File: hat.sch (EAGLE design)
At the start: 43 parts, among them U1 ADS1115IDGST, U2 ADXL345, U3 MCP2515-I/SO, U4 MCP2551, X1 16Mhz

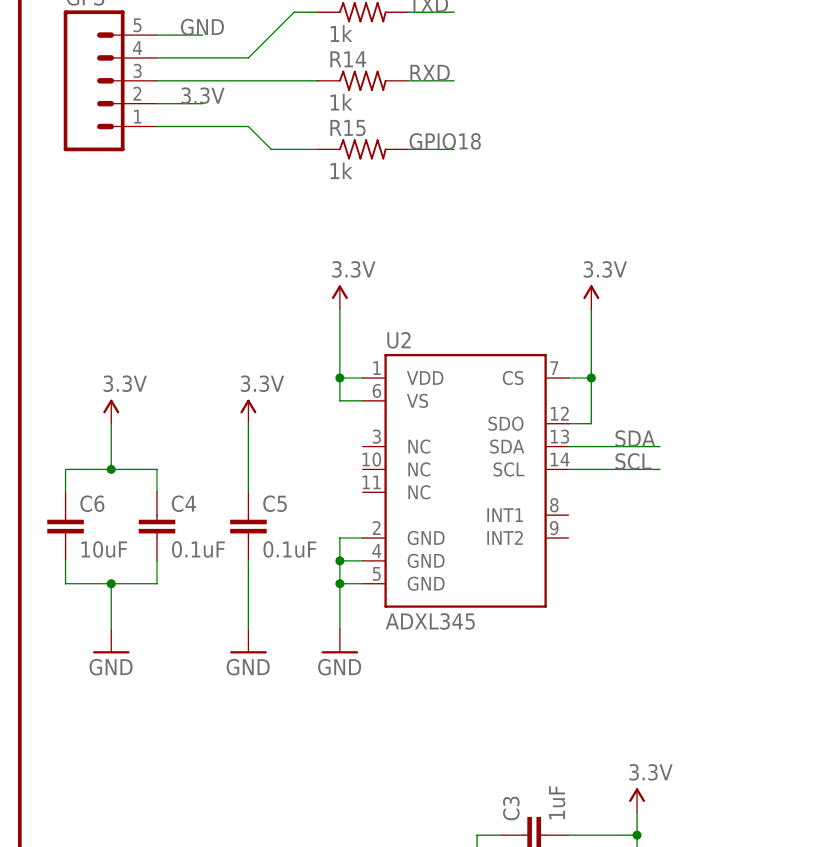
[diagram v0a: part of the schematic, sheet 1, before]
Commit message: Replaced accelerometer with i2c header
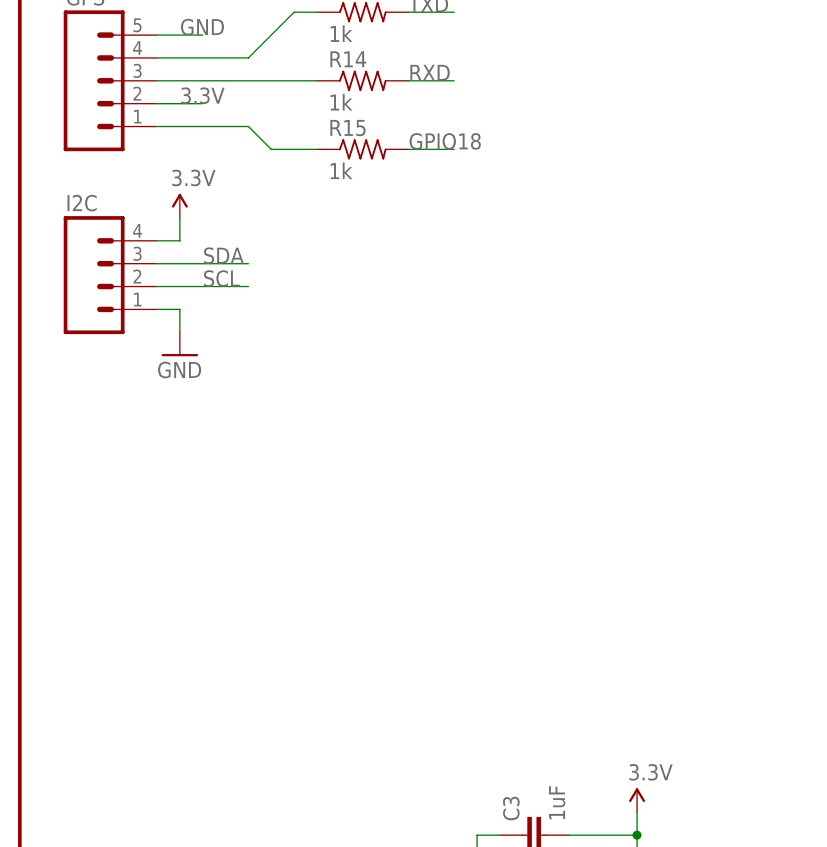
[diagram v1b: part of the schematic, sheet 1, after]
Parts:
- removed C10: 0.1uF, aceat64-passives:CAPACITOR_C0805
- removed C11, C12: 22pF, aceat64-passives:CAPACITOR_C0805
- removed U4: MCP2551, SparkFun-DigitalIC:MCP2551
- added I2C: (no value), SparkFun-Connectors:M04PTH
- C4, C5: value 0.1uF -> 560pF
- C6: value 10uF -> 0.1uF
- C7: value 560pF -> 0.1uF
- C8: value 560pF -> 22pF
- C9: value 0.1uF -> 22pF
- U2: value ADXL345 -> MCP2515-I/SO; device SparkFun-Sensors:ADXL345 -> mcp2515:MCP2515-I/SO
- U3: value MCP2515-I/SO -> MCP2551; device mcp2515:MCP2515-I/SO -> SparkFun-DigitalIC:MCP2551
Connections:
- net 3.3V: now also C7.1, I2C.4; no longer C10.1, C4.1, C5.1, C6.1, U2.CS, U2.SDO, U2.VS, U3.VDD
- net 5V: now also C6.1, U3.VSS; no longer C9.1, U4.VSS
- net CANH: now also U3.CANH; no longer U4.CANH
- net CANL: now also U3.CANL; no longer U4.CANL
- net GND: now also I2C.1, U2.VSS, U3.VDD; no longer C10.2, C11.2, C12.2, U2.GND@2, U2.GND@4, U2.GND@5, U3.VSS, U4.VDD
- net GPIO25: now also U2.INT; no longer U3.INT
- net N$14: now also C9.1, U2.OSC1; no longer C12.1, U3.OSC1
- net N$15: now also C8.1, U2.OSC2; no longer C11.1, U3.OSC2
- net N$4: now also U2.RXCAN; no longer U3.RXCAN
- net N$6: now also C4.1; no longer C7.1
- net N$8: now also C5.1; no longer C8.1
- net RS: now also U3.RS; no longer U4.RS
- net RXCAN: now also U3.RXD; no longer U4.RXD
- net SCL: now also I2C.2; no longer U2.SCL
- net SDA: now also I2C.3; no longer U2.SDA
- net SPI_CE0: now also U2.CS; no longer U3.CS
- net SPI_MISO: now also U2.SO; no longer U3.SO
- net SPI_MOSI: now also U2.SI; no longer U3.SI
- net SPI_SCLK: now also U2.SCK; no longer U3.SCK
- net TXCAN: now also U2.TXCAN, U3.TXD; no longer U3.TXCAN, U4.TXD
- net U5_RST: now also U2.RESET; no longer U3.RESET
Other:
- moved on the sheet: C7, C8, C9

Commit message: Rename U5_RST to U2_RST
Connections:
- net U5_RST renamed U2_RST
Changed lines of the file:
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@@
 <grid distance="0.1" unitdist="inch" unit="inch" style="lines" multiple="1" display="no" altdistance="0.01" altunitdist="inch" altunit="inch"/>
 <layers>
-<layer number="1" name="Top" color="4" fill="1" visible="yes" active="no"/>
-<layer number="16" name="Bottom" color="1" fill="1" visible="yes" active="no"/>
-<layer number="17" name="Pads" color="2" fill="1" visible="yes" active="no"/>
-<layer number="18" name="Vias" color="2" fill="1" visible="yes" active="no"/>
-<layer number="19" name="Unrouted" color="6" fill="1" visible="yes" active="no"/>
-<layer number="20" name="Dimension" color="15" fill="1" visible="yes" active="no"/>
-<layer number="21" name="tPlace" color="7" fill="1" visible="yes" active="no"/>
-<layer number="22" name="bPlace" color="7" fill="1" visible="yes" active="no"/>
-<layer number="23" name="tOrigins" color="15" fill="1" visible="yes" active="no"/>
-<layer number="24" name="bOrigins" color="15" fill="1" visible="yes" active="no"/>
-<layer number="25" name="tNames" color="7" fill="1" visible="yes" active="no"/>
-<layer number="26" name="bNames" color="7" fill="1" visible="yes" active="no"/>
-<layer number="27" name="tValues" color="7" fill="1" visible="yes" active="no"/>
-<layer number="28" name="bValues" color="7" fill="1" visible="yes" active="no"/>
+<layer number="1" name="Top" color="4" fill="1" visible="no" active="no"/>
+<layer number="16" name="Bottom" color="1" fill="1" visible="no" active="no"/>
+<layer number="17" name="Pads" color="2" fill="1" visible="no" active="no"/>
+<layer number="18" name="Vias" color="2" fill="1" visible="no" active="no"/>
+<layer number="19" name="Unrouted" color="6" fill="1" visible="no" active="no"/>
+<layer number="20" name="Dimension" color="15" fill="1" visible="no" active="no"/>
+<layer number="21" name="tPlace" color="7" fill="1" visible="no" active="no"/>
+<layer number="22" name="bPlace" color="7" fill="1" visible="no" active="no"/>
+<layer number="23" name="tOrigins" color="15" fill="1" visible="no" active="no"/>
+<layer number="24" name="bOrigins" color="15" fill="1" visible="no" active="no"/>
+<layer number="25" name="tNames" color="7" fill="1" visible="no" active="no"/>
+<layer number="26" name="bNames" color="7" fill="1" visible="no" active="no"/>
+<layer number="27" name="tValues" color="7" fill="1" visible="no" active="no"/>
+<layer number="28" name="bValues" color="7" fill="1" visible="no" active="no"/>
 <layer number="29" name="tStop" color="7" fill="3" visible="no" active="no"/>
 <layer number="30" name="bStop" color="7" fill="6" visible="no" active="no"/>
@@
 <layer number="35" name="tGlue" color="7" fill="4" visible="no" active="no"/>
 <layer number="36" name="bGlue" color="7" fill="5" visible="no" active="no"/>
-<layer number="37" name="tTest" color="7" fill="1" visible="yes" active="no"/>
-<layer number="38" name="bTest" color="7" fill="1" visible="yes" active="no"/>
+<layer number="37" name="tTest" color="7" fill="1" visible="no" active="no"/>
+<layer number="38" name="bTest" color="7" fill="1" visible="no" active="no"/>
 <layer number="39" name="tKeepout" color="4" fill="11" visible="no" active="no"/>
 <layer number="40" name="bKeepout" color="1" fill="11" visible="no" active="no"/>
@@
 <layer number="44" name="Drills" color="7" fill="1" visible="no" active="no"/>
 <layer number="45" name="Holes" color="7" fill="1" visible="no" active="no"/>
-<layer number="46" name="Milling" color="3" fill="1" visible="yes" active="no"/>
-<layer number="47" name="Measures" color="7" fill="1" visible="yes" active="no"/>
-<layer number="48" name="Document" color="7" fill="1" visible="yes" active="no"/>
-<layer number="49" name="Reference" color="7" fill="1" visible="yes" active="no"/>
-<layer number="50" name="dxf" color="7" fill="1" visible="yes" active="no"/>
-<layer number="51" name="tDocu" color="7" fill="1" visible="yes" active="no"/>
-<layer number="52" name="bDocu" color="7" fill="1" visible="yes" active="no"/>
-<layer number="53" name="tGND_GNDA" color="7" fill="9" visible="yes" active="no"/>
-<layer number="54" name="bGND_GNDA" color="1" fill="9" visible="yes" active="no"/>
-<layer number="56" name="wert" color="7" fill="1" visible="yes" active="no"/>
-<layer number="57" name="tCAD" color="7" fill="1" visible="yes" active="no"/>
-<layer number="59" name="tCarbon" color="7" fill="1" visible="yes" active="no"/>
-<layer number="60" name="bCarbon" color="7" fill="1" visible="yes" active="no"/>
+<layer number="46" name="Milling" color="3" fill="1" visible="no" active="no"/>
+<layer number="47" name="Measures" color="7" fill="1" visible="no" active="no"/>
+<layer number="48" name="Document" color="7" fill="1" visible="no" active="no"/>
+<layer number="49" name="Reference" color="7" fill="1" visible="no" active="no"/>
+<layer number="50" name="dxf" color="7" fill="1" visible="no" active="no"/>
+<layer number="51" name="tDocu" color="7" fill="1" visible="no" active="no"/>
+<layer number="52" name="bDocu" color="7" fill="1" visible="no" active="no"/>
+<layer number="53" name="tGND_GNDA" color="7" fill="9" visible="no" active="no"/>
+<layer number="54" name="bGND_GNDA" color="1" fill="9" visible="no" active="no"/>
+<layer number="56" name="wert" color="7" fill="1" visible="no" active="no"/>
+<layer number="57" name="tCAD" color="7" fill="1" visible="no" active="no"/>
+<layer number="59" name="tCarbon" color="7" fill="1" visible="no" active="no"/>
+<layer number="60" name="bCarbon" color="7" fill="1" visible="no" active="no"/>
 <layer number="90" name="Modules" color="5" fill="1" visible="yes" active="yes"/>
 <layer number="91" name="Nets" color="2" fill="1" visible="yes" active="yes"/>
@@
 </segment>
 </net>
-<net name="U5_RST" class="0">
+<net name="U2_RST" class="0">
 <segment>
 <wire x1="43.18" y1="114.3" x2="35.56" y2="114.3" width="0.1524" layer="91"/>

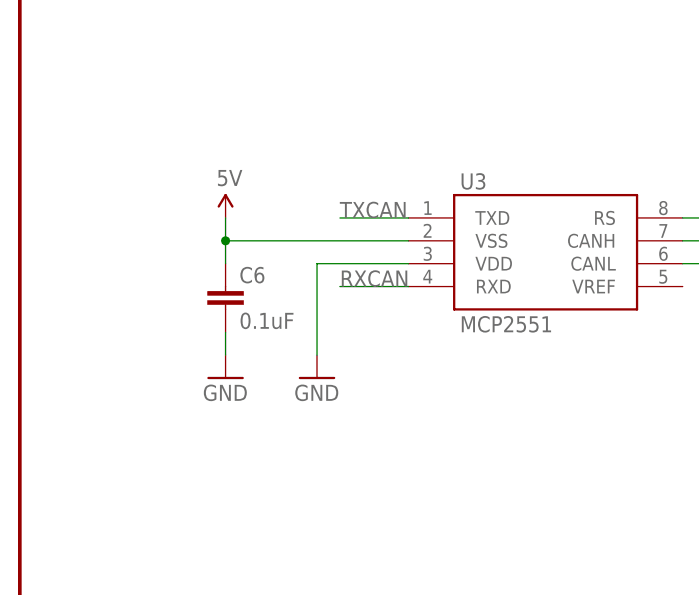
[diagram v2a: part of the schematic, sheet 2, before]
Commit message: Fixed power for MCP2551
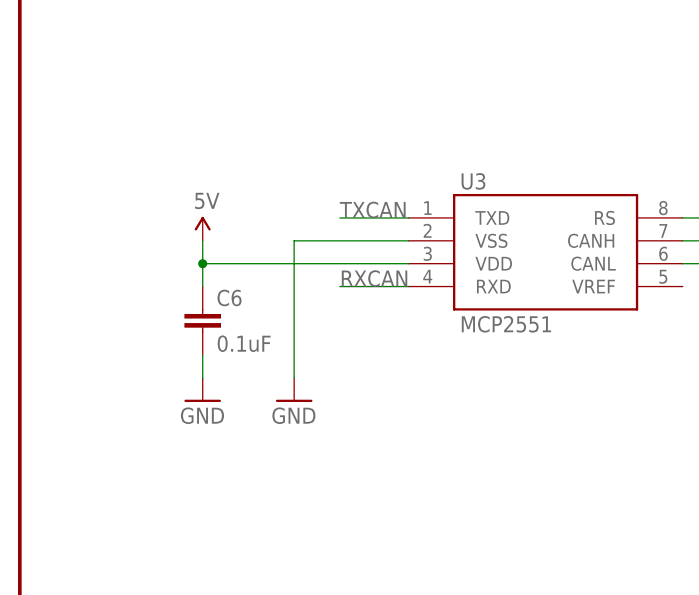
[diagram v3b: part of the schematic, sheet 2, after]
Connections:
- net 5V: now also U3.VDD; no longer U3.VSS
- net GND: now also U3.VSS; no longer U3.VDD
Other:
- moved on the sheet: C6
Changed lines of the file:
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@@
 <instance part="R8" gate="G$1" x="93.98" y="27.94" rot="R90"/>
 <instance part="R9" gate="G$1" x="106.68" y="27.94" rot="R90"/>
-<instance part="SUPPLY11" gate="G$1" x="22.86" y="45.72"/>
-<instance part="GND18" gate="1" x="22.86" y="27.94"/>
-<instance part="GND19" gate="1" x="33.02" y="27.94"/>
+<instance part="SUPPLY11" gate="G$1" x="20.32" y="43.18"/>
+<instance part="GND18" gate="1" x="20.32" y="25.4"/>
+<instance part="GND19" gate="1" x="30.48" y="25.4"/>
 <instance part="FRAME2" gate="G$1" x="0" y="0"/>
 <instance part="FRAME2" gate="V" x="147.32" y="0"/>
@@
 <instance part="C4" gate="G$1" x="93.98" y="17.78"/>
 <instance part="C5" gate="G$1" x="106.68" y="17.78"/>
-<instance part="C6" gate="G$1" x="22.86" y="38.1"/>
+<instance part="C6" gate="G$1" x="20.32" y="35.56"/>
 <instance part="C7" gate="G$1" x="83.82" y="127"/>
 <instance part="C8" gate="G$1" x="86.36" y="88.9" rot="R90"/>
@@
 <segment>
 <pinref part="GND18" gate="1" pin="GND"/>
-<wire x1="22.86" y1="30.48" x2="22.86" y2="33.02" width="0.1524" layer="91"/>
+<wire x1="20.32" y1="27.94" x2="20.32" y2="30.48" width="0.1524" layer="91"/>
 <pinref part="C6" gate="G$1" pin="2"/>
-</segment>
-<segment>
-<pinref part="U3" gate="MCP2551" pin="VDD"/>
-<wire x1="43.18" y1="40.64" x2="33.02" y2="40.64" width="0.1524" layer="91"/>
-<wire x1="33.02" y1="40.64" x2="33.02" y2="30.48" width="0.1524" layer="91"/>
-<pinref part="GND19" gate="1" pin="GND"/>
 </segment>
 <segment>
@@
 <pinref part="C8" gate="G$1" pin="2"/>
 <pinref part="C9" gate="G$1" pin="2"/>
+</segment>
+<segment>
+<pinref part="U3" gate="MCP2551" pin="VSS"/>
+<wire x1="43.18" y1="43.18" x2="30.48" y2="43.18" width="0.1524" layer="91"/>
+<pinref part="GND19" gate="1" pin="GND"/>
+<wire x1="30.48" y1="43.18" x2="30.48" y2="27.94" width="0.1524" layer="91"/>
 </segment>
 </net>
@@
 <segment>
 <pinref part="SUPPLY11" gate="G$1" pin="5V"/>
-<wire x1="22.86" y1="40.64" x2="22.86" y2="43.18" width="0.1524" layer="91"/>
-<pinref part="U3" gate="MCP2551" pin="VSS"/>
-<wire x1="22.86" y1="43.18" x2="22.86" y2="45.72" width="0.1524" layer="91"/>
-<wire x1="43.18" y1="43.18" x2="22.86" y2="43.18" width="0.1524" layer="91"/>
-<junction x="22.86" y="43.18"/>
+<wire x1="20.32" y1="38.1" x2="20.32" y2="40.64" width="0.1524" layer="91"/>
 <pinref part="C6" gate="G$1" pin="1"/>
+<pinref part="U3" gate="MCP2551" pin="VDD"/>
+<wire x1="20.32" y1="40.64" x2="20.32" y2="43.18" width="0.1524" layer="91"/>
+<wire x1="43.18" y1="40.64" x2="20.32" y2="40.64" width="0.1524" layer="91"/>
+<junction x="20.32" y="40.64"/>
 </segment>
 </net>
